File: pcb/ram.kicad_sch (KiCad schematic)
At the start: 18 parts, among them U11 HM628512, U12 HM628512, U13 HM628512, U14 HM628512, U15 HM628512, U16 HM628512, U17 HM628512, U18 HM628512, U21 W29C020

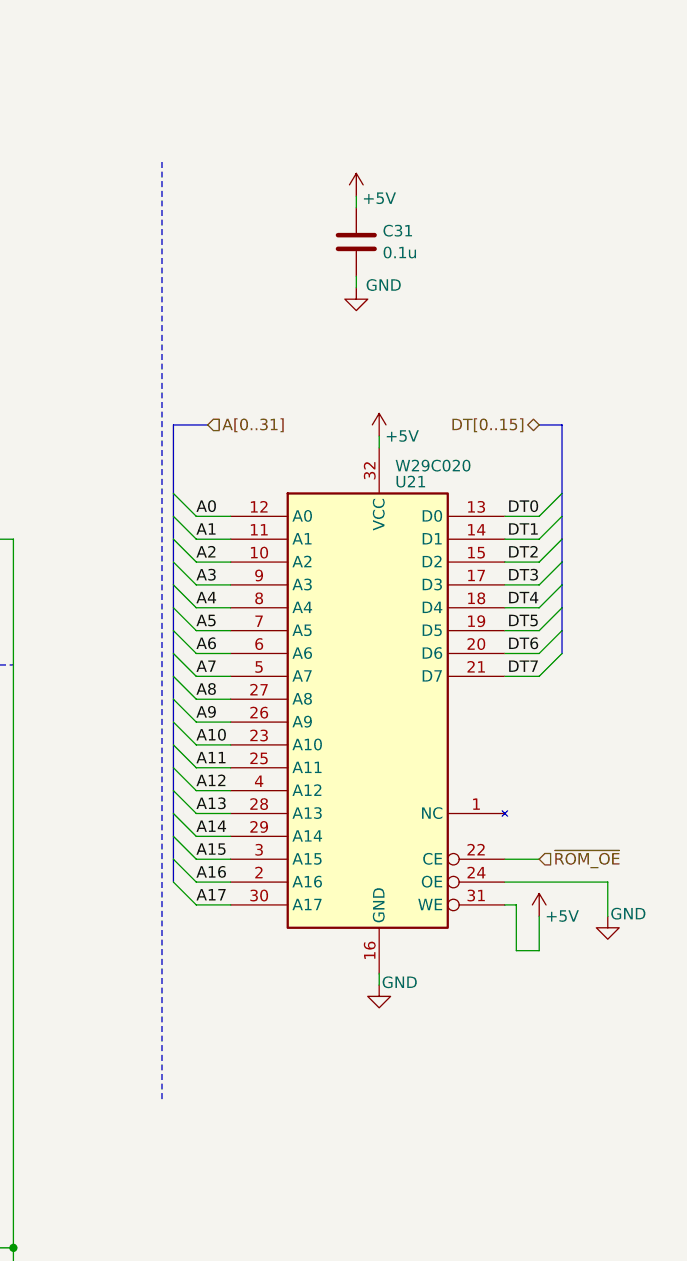
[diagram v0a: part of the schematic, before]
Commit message: moving BIOS to slow SA/DT side of CPU bus
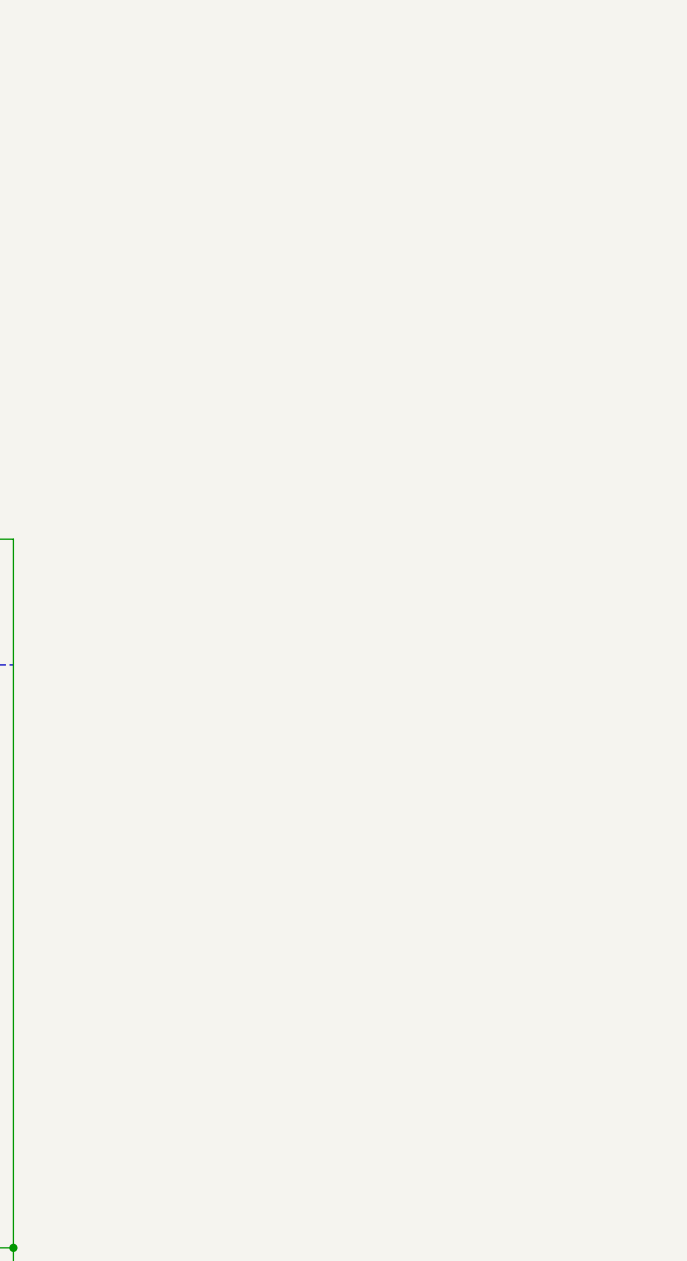
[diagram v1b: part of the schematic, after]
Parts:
- removed C31: 0.1u, Capacitor_SMD:C_0805_2012Metric_Pad1.18x1.45mm_HandSolder, symbol Device:C
- removed U21: W29C020, Package_DIP:DIP-32_W15.24mm, symbol sbc486_additional:W29C020
